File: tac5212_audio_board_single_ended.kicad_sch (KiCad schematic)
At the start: 99 parts, among them J1002 TAC5212, U108 Single Buffer - 74LVC1G125GV,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, U109 3.3v LDO - TLV74133PDBVR

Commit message: update
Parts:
- added SCL109: jumper, project_fp:jumper_slice, symbol proejct_lib:Jumper_2_Bridged
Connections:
- net 3.3v_IDE: now also SCL109.2 (B); no longer R128.2
- new net: R128.2, SCL109.1 (A)
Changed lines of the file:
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@@
 	(wire
 		(pts
+			(xy 63.5 368.3) (xy 63.5 369.57)
+		)
+		(stroke
+			(width 0)
+			(type default)
+		)
+	)
+	(wire
+		(pts
 			(xy 41.91 154.94) (xy 38.1 154.94)
 		)
@@
 	(global_label "3.3v_IDE"
 		(shape input)
-		(at 63.5 369.57 0)
+		(at 73.66 368.3 0)
 		(fields_autoplaced yes)
 		(effects
@@
 		)
 		(property "Intersheetrefs" "${INTERSHEET_REFS}"
-			(at 71.1774 369.57 0)
+			(at 81.3374 368.3 0)
 			(effects
 				(font
@@
 					(unit 1)
 				)
+			)
+		)
+	)
+	(symbol
+		(lib_id "proejct_lib:Jumper_2_Bridged")
+		(at 68.58 368.3 0)
+		(unit 1)
+		(exclude_from_sim yes)
+		(in_bom yes)
+		(on_board yes)
+		(dnp yes)
+		(property "Reference" "SCL109"
+			(at 68.58 364.998 0)
+			(effects
+				(font
+					(size 1.27 1.27)
+				)
+			)
+		)
+		(property "Value" "jumper"
+			(at 68.58 365.4044 0)
+			(effects
+				(font
+					(size 1.27 1.27)
+				)
+				(hide yes)
+			)
+		)
+		(property "Footprint" "project_fp:jumper_slice"
+			(at 68.58 368.3 0)
+			(effects
+				(font
+					(size 1.27 1.27)
+				)
+				(hide yes)
+			)
+		)
+		(property "Datasheet" "~"
+			(at 68.58 368.3 0)
+			(effects
+				(font
+					(size 1.27 1.27)
+				)
+				(hide yes)
+			)
+		)
+		(property "Description" "Jumper, open"
+			(at 68.58 368.3 0)
+			(effects
+				(font
+					(size 1.27 1.27)
+				)
+				(hide yes)
+			)
+		)
+		(property "Label" "SC"
+			(at 68.58 368.3 0)
+			(effects
+				(font
+					(size 1.27 1.27)
+				)
+				(hide yes)
+			)
+		)
+		(property "Package / Case" "DNP"
+			(at 68.58 368.3 0)
+			(effects
+				(font
+					(size 1.27 1.27)
+				)
+				(hide yes)
+			)
+		)
+		(property "TAC5212EVM" "n/a"
+			(at 68.58 368.3 0)
+			(effects
+				(font
+					(size 1.27 1.27)
+				)
+				(hide yes)
+			)
+		)
+		(property "REPLACE FOR NEXT BUILD" ""
+			(at 68.58 368.3 0)
+			(effects
+				(font
+					(size 1.27 1.27)
+				)
+				(hide yes)
+			)
+		)
+		(pin "1"
+		)
+		(pin "2"
+		)
+		(instances
+			(project "tac5212_audio_board_single_ended"
+				(path "/8cee3af6-3893-45a9-89a4-21657973eeff"
+					(reference "SCL109")
+					(unit 1)
+				)

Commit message: update
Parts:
- added NT108, NT109: NetTie_2, project_fp:NetTie-2_SMD_Pad0.2mm, symbol Device:NetTie_2
- D116: footprint project_fp:R_0805_2012Metric_Pad1.20x1.40mm_HandSolder -> project_fp:D_0805_2012Metric_custom
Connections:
- net 3.3V_LDO: now also NT109.1; no longer C1001.1, C1006.1, TAC108-Q1.31 (AVDD)
- net 3.3v_IDE: now also J1002.6 (IOVDD)
- net 5212_SCL: no longer J1002.7 (SCL)
- net 5212_SDA: no longer J1002.8 (SDA)
- net 5V: now also NT108.1; no longer T*C108.1, T*C109.1, U109.1 (IN)
- net Earth: now also G119.1 (A); no longer G119.2 (B)
- net GNDD: now also TAC108-Q1.15 (BSTVSS); no longer TAC108-Q1. (VSS)
- net MICBIAS: now also J1002.14 (MICBIAS)
- net OUT1M: now also J1002.19 (OUT1M)
- net at R1006.2: now also J1002.11 (GPO1), TAC108-Q1.23 (GPO1A); no longer TAC108-Q1.11 (GPO1)
- net at T*C108.2, T*C109.2, T*C110.2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: now also G119.2 (B); no longer G119.1 (A)
- net at C1004.2, TAC108-Q1.32 (VREF): now also J1002.24 (VREF)
- net at C1003.1, C1005.1, TAC108-Q1.2 (DREG): now also J1002.1 (DREG)
- net at R1007.2, TAC108-Q1.24 (GPI2A): now also J1002.10 (GPIO2)
- net at ADD1001.2, ADD1002.2, ADD1003.2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: no longer J1002.13 (ADDR)
- net at J1002.9 (GPIO1), R1008.2: now also TAC108-Q1.11 (GPIO1); no longer TAC108-Q1.23 (GPIO1)
- net at R1005.2, TAC108-Q1.25 (GPI1A): now also J1002.12 (GPI1)
- net 3.3V_THIN: now reaches J1002.23 (AVDD)
- net 3.3V_THIN: now also C1001.1, C1006.1, TAC108-Q1.31 (AVDD), NT109.2
- new net 5V_THIN: NT108.2, T*C108.1, T*C109.1, U109.1 (IN)
- no-connect marks 7 -> 6
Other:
- moved on the sheet: ADD1001, ADD1002, ADD1003, ADD1004, C1009, C1010, C1011, C1012, C1013, C1014, C1015, C1016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

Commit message: update
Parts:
- MCLK108: footprint project_fp:jumper_slice_disconnected -> Jumper:SolderJumper-2_P1.3mm_Open_Pad1.0x1.5mm
- SCL109: footprint project_fp:jumper_slice -> Resistor_SMD:R_0402_1005Metric_Pad0.72x0.64mm_HandSolder; symbol proejct_lib:Jumper_2_Bridged -> proejct_lib:Jumper_NO_Small-Device
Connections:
- net 5212_DIN1: now also board_outline108.7 (DSP_DOUT); no longer board_outline108.9 (DSP_DIN)
- net 5212_DOUT1+: now also board_outline108.9 (DSP_DIN); no longer board_outline108.7 (DSP_DOUT)
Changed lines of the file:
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@@
 	(wire
 		(pts
+			(xy 63.5 336.55) (xy 66.04 336.55)
+		)
+		(stroke
+			(width 0)
+			(type default)
+		)
+	)
+	(wire
+		(pts
 			(xy 97.79 355.6) (xy 101.6 355.6)
 		)
@@
 	(wire
 		(pts
+			(xy 71.12 336.55) (xy 73.66 336.55)
+		)
+		(stroke
+			(width 0)
+			(type default)
+		)
+	)
+	(wire
+		(pts
 			(xy 346.71 181.61) (xy 341.63 181.61)
 		)
@@
 	(global_label "5212_DOUT1+"
 		(shape input)
-		(at 66.04 231.14 180)
+		(at 66.04 233.68 180)
 		(fields_autoplaced yes)
 		(effects
@@
 		)
 		(property "Intersheetrefs" "${INTERSHEET_REFS}"
-			(at 55.6645 231.14 0)
+			(at 55.6645 233.68 0)
 			(effects
 				(font
@@
 	(global_label "5212_DIN1"
 		(shape input)
-		(at 66.04 233.68 180)
+		(at 66.04 231.14 180)
 		(fields_autoplaced yes)
 		(effects
@@
 		)
 		(property "Intersheetrefs" "${INTERSHEET_REFS}"
-			(at 57.7216 233.68 0)
+			(at 57.7216 231.14 0)
 			(effects
 				(font
@@
 			)
 		)
-		(property "Footprint" "project_fp:jumper_slice_disconnected"
+		(property "Footprint" "Jumper:SolderJumper-2_P1.3mm_Open_Pad1.0x1.5mm"
 			(at 46.99 127 0)
 			(effects
@@
 	)
 	(symbol
-		(lib_id "proejct_lib:Jumper_2_Bridged")
+		(lib_id "proejct_lib:Jumper_NO_Small-Device")
 		(at 68.58 336.55 0)
 		(unit 1)
-		(exclude_from_sim yes)
+		(exclude_from_sim no)
 		(in_bom yes)
 		(on_board yes)
@@
 			)
 		)
-		(property "Footprint" "project_fp:jumper_slice"
+		(property "Footprint" "Resistor_SMD:R_0402_1005Metric_Pad0.72x0.64mm_HandSolder"
 			(at 68.58 336.55 0)
 			(effects
@@
 			)
 		)
-		(property "Description" "Jumper, open"
+		(property "Description" "Jumper, 2-pole, open"
 			(at 68.58 336.55 0)
 			(effects

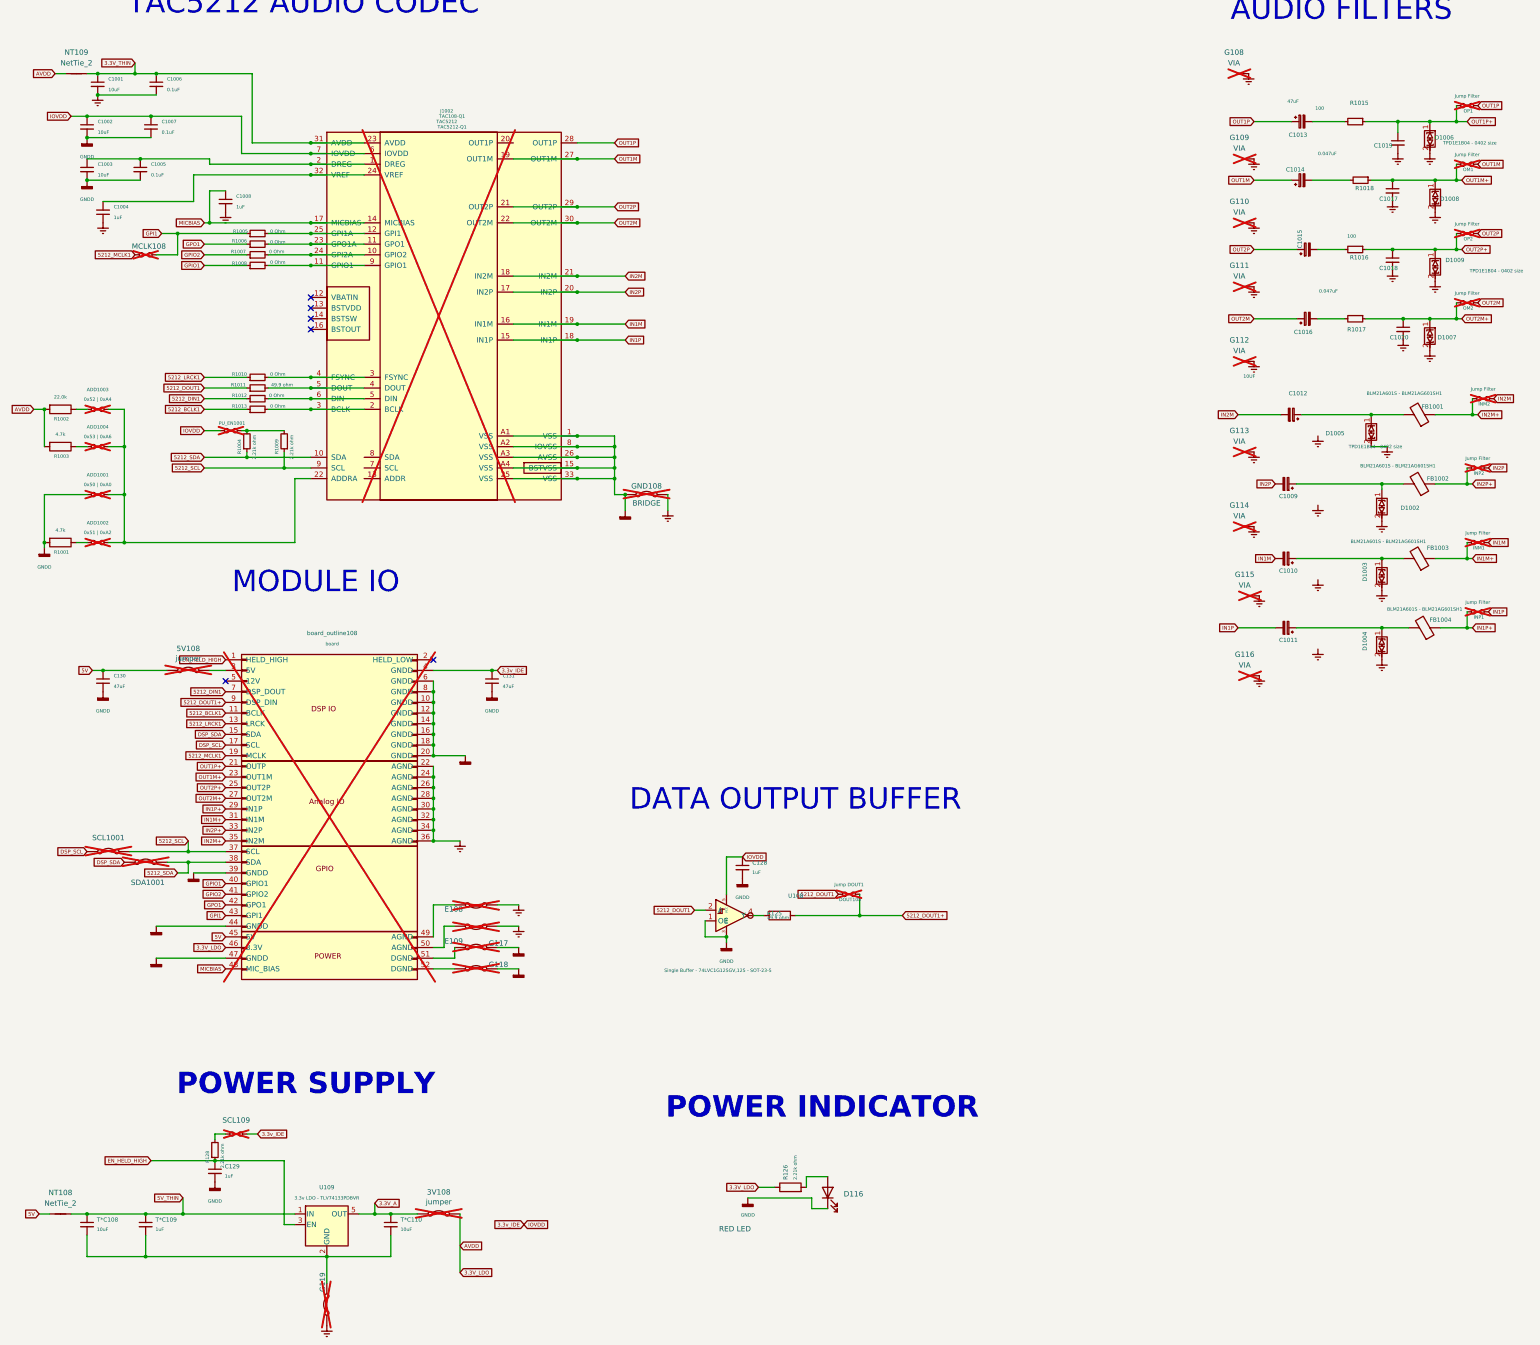
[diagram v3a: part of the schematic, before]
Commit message: fix net ties and 28 pin wqfn-28
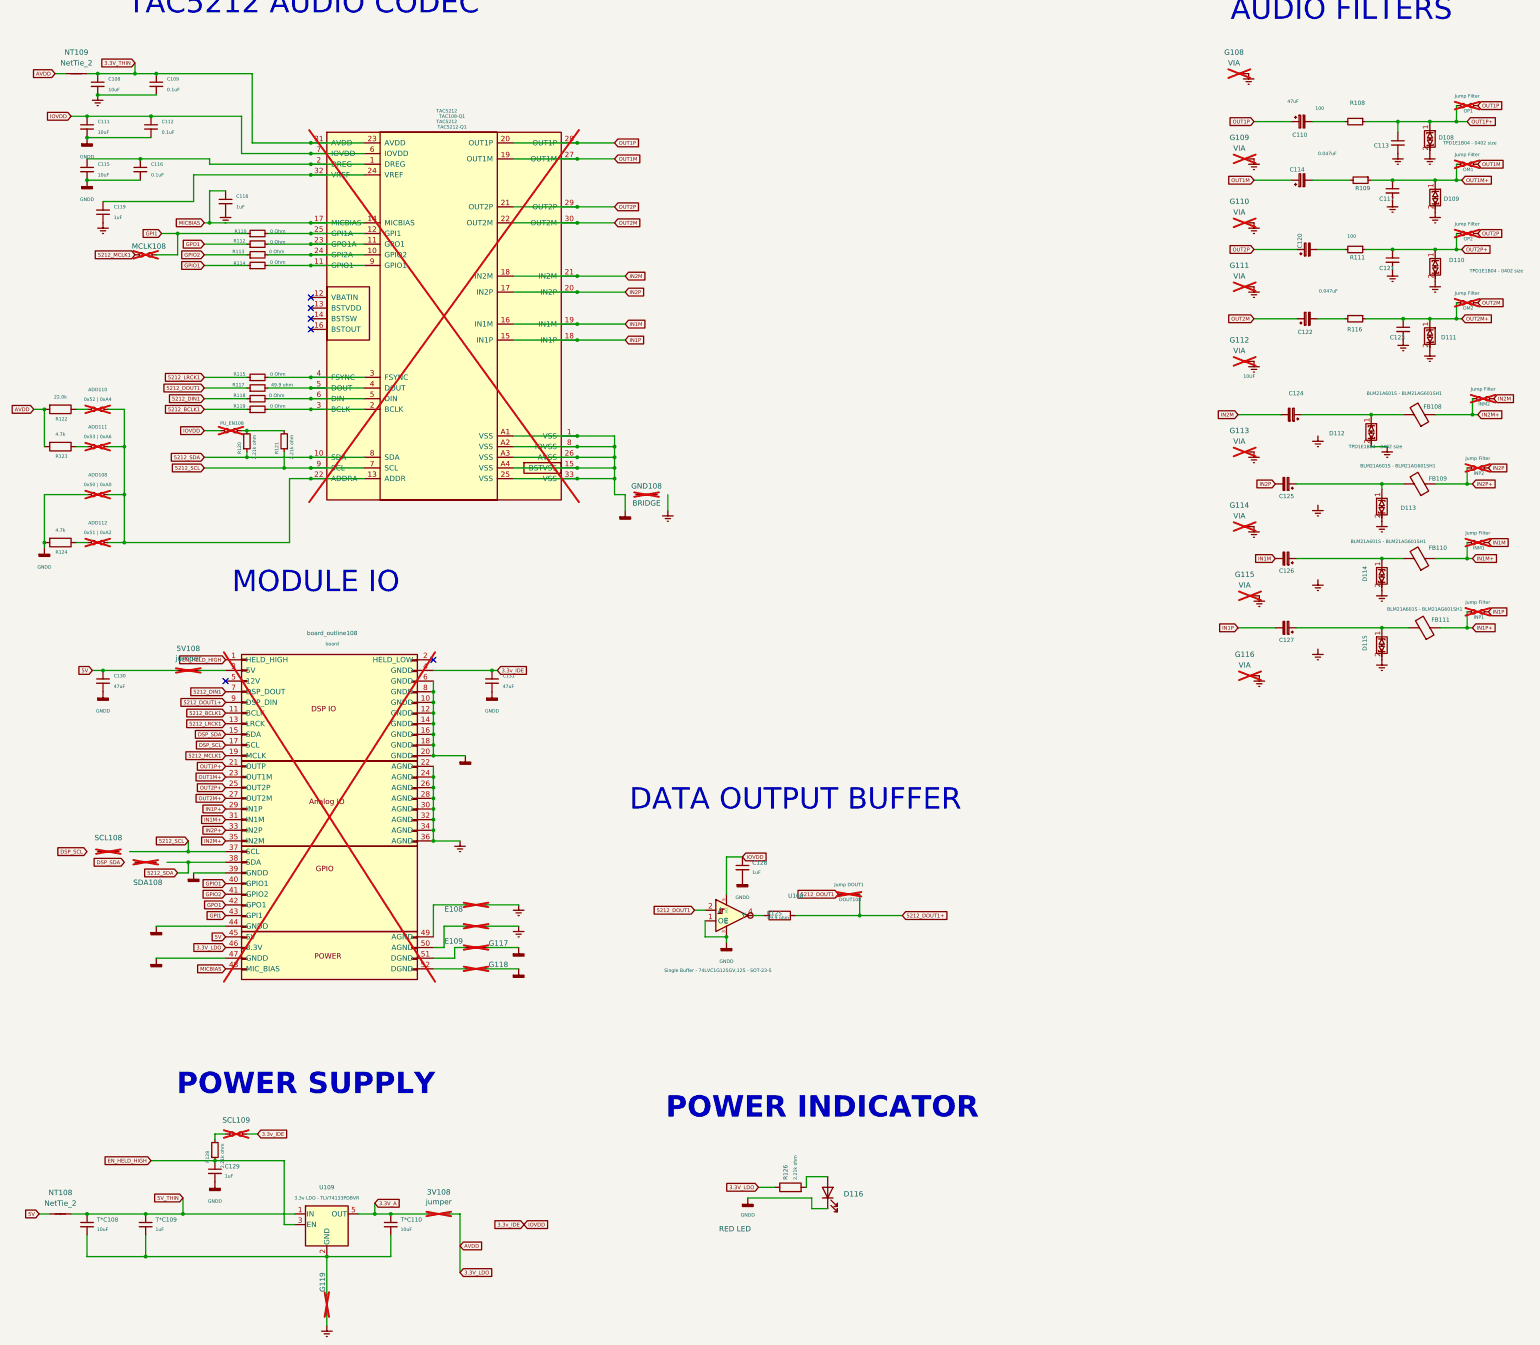
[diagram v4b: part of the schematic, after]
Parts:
- 3V108, 5V108, E108, E109, G117, G118, G119, GND108: symbol proejct_lib:Jumper_2_Bridged -> Device:NetTie_2; now left out of the parts list
- C109: renamed from C1006; footprint Capacitor_SMD:C_0402_1005Metric -> project_fp:C_0402_1005Metric
- C110: renamed from C1013; footprint Capacitor_Tantalum_SMD:CP_EIA-3528-21_Kemet-B_Pad1.50x2.35mm_HandSolder -> project_fp:CP_EIA-3528-21_Kemet-B_Pad1.50x2.35mm_HandSolder
- C112: renamed from C1007; footprint Capacitor_SMD:C_0402_1005Metric -> project_fp:C_0402_1005Metric
- C113: renamed from C1019; footprint Capacitor_SMD:C_0603_1608Metric_Pad1.08x0.95mm_HandSolder -> project_fp:C_0603_1608Metric_Pad1.08x0.95mm_HandSolder
- C114: renamed from C1014; footprint Capacitor_Tantalum_SMD:CP_EIA-3528-21_Kemet-B_Pad1.50x2.35mm_HandSolder -> project_fp:CP_EIA-3528-21_Kemet-B_Pad1.50x2.35mm_HandSolder
- C116: renamed from C1005; footprint Capacitor_SMD:C_0402_1005Metric -> project_fp:C_0402_1005Metric
- C117: renamed from C1017; footprint Capacitor_SMD:C_0603_1608Metric_Pad1.08x0.95mm_HandSolder -> project_fp:C_0603_1608Metric_Pad1.08x0.95mm_HandSolder
- C118: renamed from C1008; footprint Capacitor_SMD:C_0603_1608Metric_Pad1.08x0.95mm_HandSolder -> project_fp:C_0603_1608Metric_Pad1.08x0.95mm_HandSolder
- C119: renamed from C1004; footprint Capacitor_SMD:C_0603_1608Metric_Pad1.08x0.95mm_HandSolder -> project_fp:C_0603_1608Metric_Pad1.08x0.95mm_HandSolder
- C120: renamed from C1015; footprint Capacitor_Tantalum_SMD:CP_EIA-3528-21_Kemet-B_Pad1.50x2.35mm_HandSolder -> project_fp:CP_EIA-3528-21_Kemet-B_Pad1.50x2.35mm_HandSolder
- C121: renamed from C1018; footprint Capacitor_SMD:C_0603_1608Metric_Pad1.08x0.95mm_HandSolder -> project_fp:C_0603_1608Metric_Pad1.08x0.95mm_HandSolder
- C122: renamed from C1016; footprint Capacitor_Tantalum_SMD:CP_EIA-3528-21_Kemet-B_Pad1.50x2.35mm_HandSolder -> project_fp:CP_EIA-3528-21_Kemet-B_Pad1.50x2.35mm_HandSolder
- C123: renamed from C1020; footprint Capacitor_SMD:C_0603_1608Metric_Pad1.08x0.95mm_HandSolder -> project_fp:C_0603_1608Metric_Pad1.08x0.95mm_HandSolder
- C124: renamed from C1012; footprint Capacitor_SMD:C_0603_1608Metric_Pad1.08x0.95mm_HandSolder -> project_fp:C_0603_1608Metric_Pad1.08x0.95mm_HandSolder
- C125: renamed from C1009; footprint Capacitor_SMD:C_0603_1608Metric_Pad1.08x0.95mm_HandSolder -> project_fp:C_0603_1608Metric_Pad1.08x0.95mm_HandSolder
- C126: renamed from C1010; footprint Capacitor_SMD:C_0603_1608Metric_Pad1.08x0.95mm_HandSolder -> project_fp:C_0603_1608Metric_Pad1.08x0.95mm_HandSolder
- C127: renamed from C1011; footprint Capacitor_SMD:C_0603_1608Metric_Pad1.08x0.95mm_HandSolder -> project_fp:C_0603_1608Metric_Pad1.08x0.95mm_HandSolder
- C128, C129, T*C109: footprint Capacitor_SMD:C_0603_1608Metric_Pad1.08x0.95mm_HandSolder -> project_fp:C_0603_1608Metric_Pad1.08x0.95mm_HandSolder
- DOUT108: symbol proejct_lib:Jumper_NO_Small-Device -> Device:NetTie_2
- R110: renamed from R1005; footprint Resistor_SMD:R_0402_1005Metric_Pad0.72x0.64mm_HandSolder -> project_fp:R_0402_1005Metric_Pad0.72x0.64mm_HandSolder
- R112: renamed from R1006; footprint Resistor_SMD:R_0402_1005Metric_Pad0.72x0.64mm_HandSolder -> project_fp:R_0402_1005Metric_Pad0.72x0.64mm_HandSolder
- R113: renamed from R1007; footprint Resistor_SMD:R_0402_1005Metric_Pad0.72x0.64mm_HandSolder -> project_fp:R_0402_1005Metric_Pad0.72x0.64mm_HandSolder
- R114: renamed from R1008; footprint Resistor_SMD:R_0402_1005Metric_Pad0.72x0.64mm_HandSolder -> project_fp:R_0402_1005Metric_Pad0.72x0.64mm_HandSolder
- R115: renamed from R1010; footprint Resistor_SMD:R_0402_1005Metric_Pad0.72x0.64mm_HandSolder -> project_fp:R_0402_1005Metric_Pad0.72x0.64mm_HandSolder
- R117: renamed from R1011; footprint Resistor_SMD:R_0402_1005Metric_Pad0.72x0.64mm_HandSolder -> project_fp:R_0402_1005Metric_Pad0.72x0.64mm_HandSolder
- R118: renamed from R1012; footprint Resistor_SMD:R_0402_1005Metric_Pad0.72x0.64mm_HandSolder -> project_fp:R_0402_1005Metric_Pad0.72x0.64mm_HandSolder
- R119: renamed from R1013; footprint Resistor_SMD:R_0402_1005Metric_Pad0.72x0.64mm_HandSolder -> project_fp:R_0402_1005Metric_Pad0.72x0.64mm_HandSolder
- R120: renamed from R1004; footprint Resistor_SMD:R_0402_1005Metric -> project_fp:R_0402_1005Metric
- R121: renamed from R1009; footprint Resistor_SMD:R_0402_1005Metric -> project_fp:R_0402_1005Metric
- R122: renamed from R1002; footprint Resistor_SMD:R_0402_1005Metric -> project_fp:R_0402_1005Metric
- R123: renamed from R1003; footprint Resistor_SMD:R_0402_1005Metric -> project_fp:R_0402_1005Metric
- R124: renamed from R1001; footprint Resistor_SMD:R_0402_1005Metric -> project_fp:R_0402_1005Metric
- R125: footprint Resistor_SMD:R_0402_1005Metric_Pad0.72x0.64mm_HandSolder -> project_fp:R_0402_1005Metric_Pad0.72x0.64mm_HandSolder
- R126, R128: footprint Resistor_SMD:R_0402_1005Metric -> project_fp:R_0402_1005Metric
- SCL108: renamed from SCL1001; symbol proejct_lib:Jumper_2_Bridged -> Device:NetTie_2; now left out of the parts list
- SDA108: renamed from SDA1001; symbol proejct_lib:Jumper_2_Bridged -> Device:NetTie_2; now left out of the parts list
- TAC108-Q1: now not fitted
- TAC5212: renamed from J1002; now fitted
- renumbered ADD1001 to ADD108, ADD1003 to ADD110, ADD1004 to ADD111, ADD1002 to ADD112, C1001 to C108, C1002 to C111, C1003 to C115, D1006 to D108, D1008 to D109, D1009 to D110, D1007 to D111, D1005 to D112, D1002 to D113, D1003 to D114, D1004 to D115, FB1001 to FB108, FB1002 to FB109, FB1003 to FB110, FB1004 to FB111, PU_EN1001 to PU_EN108, R1015 to R108, R1018 to R109, R1016 to R111, R1017 to R116
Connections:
- net 5212_SCL: now also TAC5212.7 (SCL); no longer SCL108.2 (B)
- net 5212_SDA: now also TAC5212.8 (SDA); no longer SDA108.2 (B)
- net DSP_SCL: no longer SCL108.1 (A)
- net DSP_SDA: no longer SDA108.1 (A)
- net Earth: no longer GND108.2 (B)
- net GNDD: no longer GND108.1 (A)
- net OUT1P: now also TAC5212.20 (OUT1P)
- net at ADD108.2, ADD110.2, ADD111.2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: now also TAC5212.13 (ADDR)
